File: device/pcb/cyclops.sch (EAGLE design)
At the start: 180 parts, among them Q1 SSM3K324, Q2 SSM3K324, Q3 SSM3K324, Q4 IRF510, U1 MCP4921, U10 ADG1201, U11 THS4281, U12 MAX4564, U13 ZXTD, U14 ZXTD, U15 OPA1664, U2 LT1931, U3 LT1764A, U31 TPS62153, U4 BD00IA5WEFJ, U5 TPS72325, U6 LT1711, U7 TLV3701, U8 ADR03, U9 LT1880

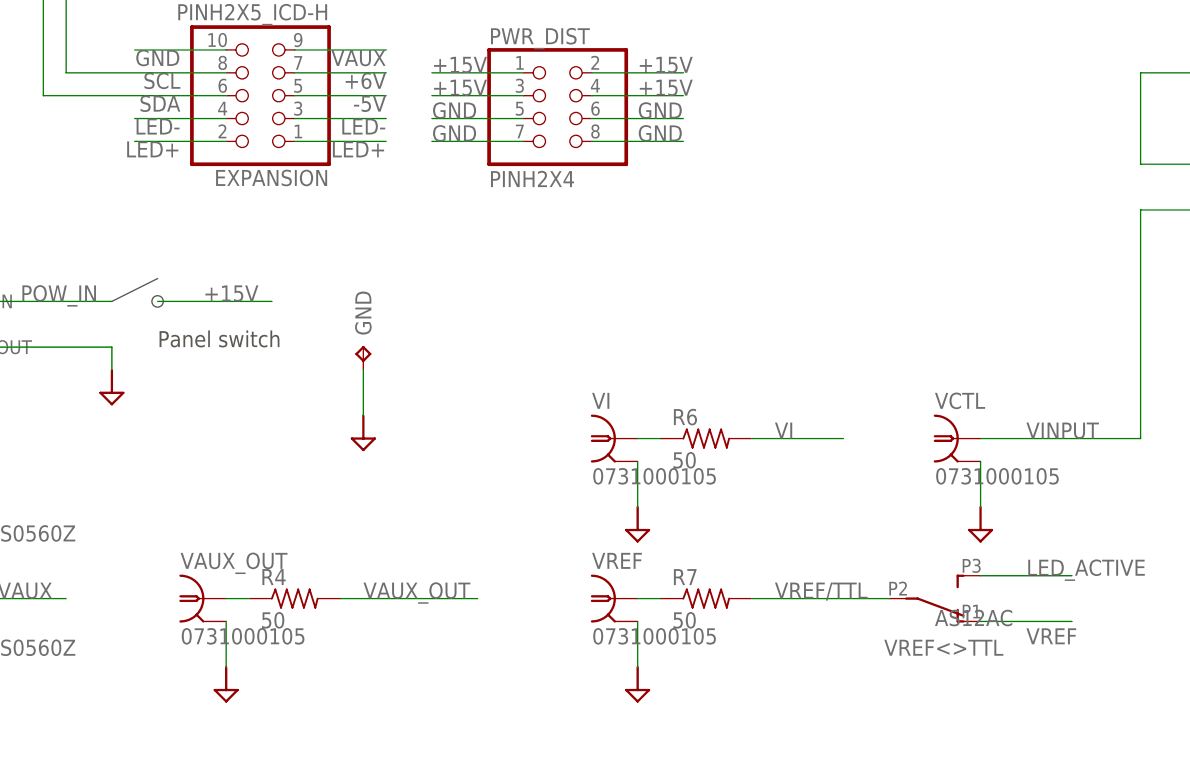
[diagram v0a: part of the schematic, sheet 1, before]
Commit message: Fixed a few minor issues found during circuit hub uploading process.
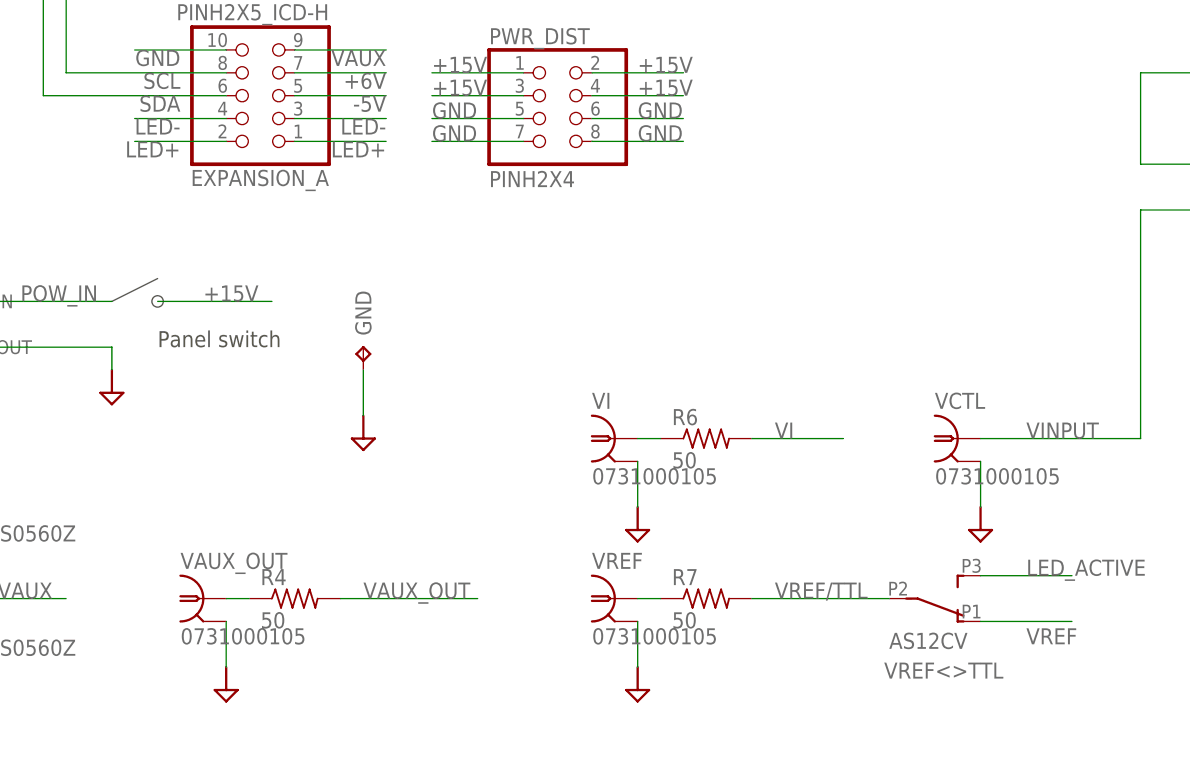
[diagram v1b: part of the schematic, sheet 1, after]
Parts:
- U4: value BD00IA5WEFJ -> BD00FC0WEFJ
- VREF<>TTL: value AS12AC -> AS12CV
- renumbered EXPANSION to EXPANSION_A
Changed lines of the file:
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@@
 <part name="GAIN" library="cyclops" deviceset="POT_US" device="_3310" value="1k"/>
 <part name="VCTL&lt;OFF&gt;DAC" library="cyclops" deviceset="SPDT" device="_2M-WITHOFF" value="100-SP3"/>
-<part name="EXPANSION" library="cyclops" deviceset="PINH2X5" device="_ICD-H"/>
+<part name="EXPANSION_A" library="cyclops" deviceset="PINH2X5" device="_ICD-H"/>
 <part name="VAUX_IN" library="jonnew" deviceset="BNC" device="_0731000105" value="0731000105"/>
 <part name="U$1" library="cyclops" deviceset="GND2" device=""/>
@@
 <part name="OC" library="jonnew" deviceset="LED_2X" device="_VERTICAL" value="569-0112-200"/>
 <part name="D2" library="jonnew" deviceset="S-DIODE" device="SOD-123" value="1N5819"/>
-<part name="VREF&lt;&gt;TTL" library="jonnew" deviceset="SPDT" device="_AS12A*" value="AS12AC"/>
+<part name="VREF&lt;&gt;TTL" library="jonnew" deviceset="SPDT" device="_AS12A*" value="AS12CV"/>
 <part name="C20" library="cyclops" deviceset="C" device="_0603" value=".1uF"/>
 <part name="R27" library="cyclops" deviceset="R" device="_0603" value="1k"/>
@@
 <part name="R6" library="jonnew" deviceset="R" device="_1206" value="50"/>
 <part name="R7" library="jonnew" deviceset="R" device="_1206" value="50"/>
-<part name="U4" library="jonnew" deviceset="LDO_ADJUST" device="_BDXXFC0" value="BD00IA5WEFJ"/>
+<part name="U4" library="jonnew" deviceset="LDO_ADJUST" device="_BDXXFC0" value="BD00FC0WEFJ"/>
 <part name="P+8" library="cyclops" deviceset="+5V" device="" value="+5V"/>
 <part name="P+16" library="jonnew" deviceset="+5V" device="" value="+6V"/>
@@
 <attribute name="VALUE" x="180.34" y="-11.43" size="1.778" layer="96" rot="MR180"/>
 </instance>
-<instance part="EXPANSION" gate="G$1" x="55.88" y="5.08" rot="R180"/>
+<instance part="EXPANSION_A" gate="G$1" x="55.88" y="5.08" rot="R180"/>
 <instance part="VAUX_IN" gate="G$1" x="5.08" y="-50.8"/>
 <instance part="P+2" gate="1" x="185.42" y="81.28"/>
@@
 <instance part="D2" gate="G$1" x="139.7" y="129.54" rot="R180"/>
 <instance part="VREF&lt;&gt;TTL" gate="G$1" x="129.54" y="-50.8" smashed="yes" rot="MR180">
-<attribute name="NAME" x="139.7" y="-57.15" size="1.778" layer="95" rot="MR0"/>
-<attribute name="VALUE" x="132.08" y="-52.07" size="1.778" layer="96" rot="MR180"/>
+<attribute name="NAME" x="139.7" y="-59.69" size="1.778" layer="95" rot="MR0"/>
+<attribute name="VALUE" x="127" y="-54.61" size="1.778" layer="96" rot="MR180"/>
 </instance>
 <instance part="UC" gate="G$1" x="93.98" y="99.06"/>
@@
 </segment>
 <segment>
-<pinref part="EXPANSION" gate="G$1" pin="10"/>
+<pinref part="EXPANSION_A" gate="G$1" pin="10"/>
 <wire x1="53.34" y1="10.16" x2="43.18" y2="10.16" width="0.1524" layer="91"/>
 <label x="48.26" y="10.16" size="1.778" layer="95" rot="R180"/>
@@
 </segment>
 <segment>
-<pinref part="EXPANSION" gate="G$1" pin="9"/>
+<pinref part="EXPANSION_A" gate="G$1" pin="9"/>
 <wire x1="60.96" y1="10.16" x2="71.12" y2="10.16" width="0.1524" layer="91"/>
 <label x="71.12" y="10.16" size="1.778" layer="95" rot="R180"/>
@@
 <net name="-5V" class="0">
 <segment>
-<pinref part="EXPANSION" gate="G$1" pin="5"/>
+<pinref part="EXPANSION_A" gate="G$1" pin="5"/>
 <wire x1="60.96" y1="5.08" x2="71.12" y2="5.08" width="0.1524" layer="91"/>
 <label x="71.12" y="5.08" size="1.778" layer="95" rot="R180"/>
@@
 <net name="LED-" class="0">
 <segment>
-<pinref part="EXPANSION" gate="G$1" pin="3"/>
+<pinref part="EXPANSION_A" gate="G$1" pin="3"/>
 <wire x1="60.96" y1="2.54" x2="71.12" y2="2.54" width="0.1524" layer="91"/>
 <label x="71.12" y="2.54" size="1.778" layer="95" rot="R180"/>
 </segment>
 <segment>
-<pinref part="EXPANSION" gate="G$1" pin="4"/>
+<pinref part="EXPANSION_A" gate="G$1" pin="4"/>
 <wire x1="53.34" y1="2.54" x2="43.18" y2="2.54" width="0.1524" layer="91"/>
 <label x="48.26" y="2.54" size="1.778" layer="95" rot="R180"/>
@@
 <wire x1="33.02" y1="40.64" x2="33.02" y2="25.4" width="0.1524" layer="91"/>
 <wire x1="33.02" y1="5.08" x2="33.02" y2="25.4" width="0.1524" layer="91"/>
-<pinref part="EXPANSION" gate="G$1" pin="6"/>
+<pinref part="EXPANSION_A" gate="G$1" pin="6"/>
 <wire x1="53.34" y1="5.08" x2="33.02" y2="5.08" width="0.1524" layer="91"/>
 <label x="48.26" y="5.08" size="1.778" layer="95" rot="R180"/>
@@
 <wire x1="35.56" y1="40.64" x2="35.56" y2="33.02" width="0.1524" layer="91"/>
 <wire x1="35.56" y1="33.02" x2="35.56" y2="7.62" width="0.1524" layer="91"/>
-<pinref part="EXPANSION" gate="G$1" pin="8"/>
+<pinref part="EXPANSION_A" gate="G$1" pin="8"/>
 <wire x1="53.34" y1="7.62" x2="35.56" y2="7.62" width="0.1524" layer="91"/>
 <label x="48.26" y="7.62" size="1.778" layer="95" rot="R180"/>
@@
 <net name="LED+" class="0">
 <segment>
-<pinref part="EXPANSION" gate="G$1" pin="2"/>
+<pinref part="EXPANSION_A" gate="G$1" pin="2"/>
 <wire x1="53.34" y1="0" x2="43.18" y2="0" width="0.1524" layer="91"/>
 <label x="48.26" y="0" size="1.778" layer="95" rot="R180"/>
 </segment>
 <segment>
-<pinref part="EXPANSION" gate="G$1" pin="1"/>
+<pinref part="EXPANSION_A" gate="G$1" pin="1"/>
 <wire x1="60.96" y1="0" x2="71.12" y2="0" width="0.1524" layer="91"/>
 <label x="71.12" y="0" size="1.778" layer="95" rot="R180"/>
@@
 </segment>
 <segment>
-<pinref part="EXPANSION" gate="G$1" pin="7"/>
+<pinref part="EXPANSION_A" gate="G$1" pin="7"/>
 <wire x1="60.96" y1="7.62" x2="71.12" y2="7.62" width="0.1524" layer="91"/>
 <label x="71.12" y="7.62" size="1.778" layer="95" rot="R180"/>

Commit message: Minor changes prior to fab of 3.6 alpha.
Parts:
- PWR_DIST: value PINH2X4 -> SSQ-104-03-G-D
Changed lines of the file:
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@@
 <part name="VREF" library="jonnew" deviceset="BNC" device="_0731000105" value="0731000105"/>
 <part name="VCTL" library="jonnew" deviceset="BNC" device="_0731000105" value="0731000105"/>
-<part name="PWR_DIST" library="cyclops" deviceset="PINH2X4" device=""/>
+<part name="PWR_DIST" library="cyclops" deviceset="PINH2X4" device="" value="SSQ-104-03-G-D"/>
 <part name="GAIN" library="cyclops" deviceset="POT_US" device="_3310" value="1k"/>
 <part name="VCTL&lt;OFF&gt;DAC" library="cyclops" deviceset="SPDT" device="_2M-WITHOFF" value="100-SP3"/>
